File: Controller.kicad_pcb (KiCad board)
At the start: 4 copper layers, 180 x 80 mm, 39 parts, among them J1 I2C1, J10 I2C2, J11 MOTOR0_PWR, J12 MOTOR1_PWR, J13 MOTOR2_PWR, J14 MOTOR3_PWR, J15 MOTOR4_PWR, J16 MOTOR5_PWR, J17 ARM0_ROT, J18 ARM0_GRB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

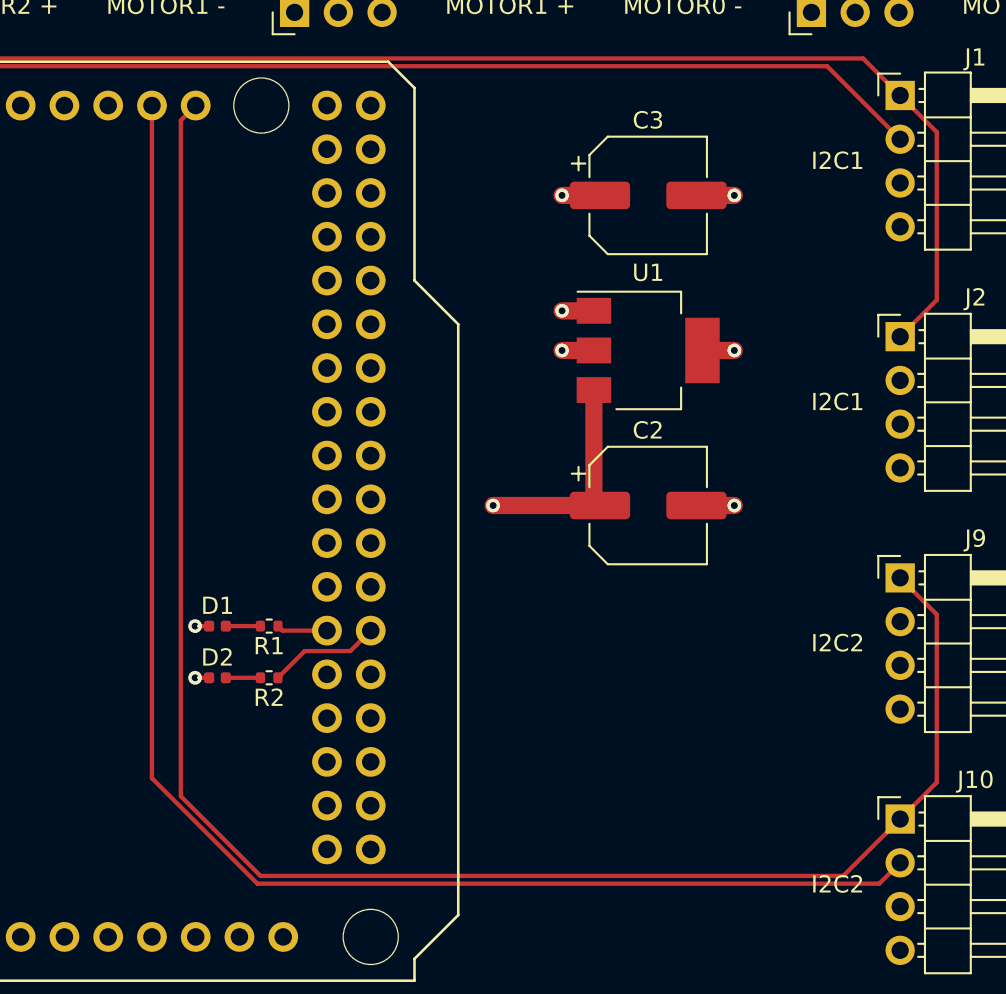
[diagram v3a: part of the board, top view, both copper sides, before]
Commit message: Use 0603 resistors and LED
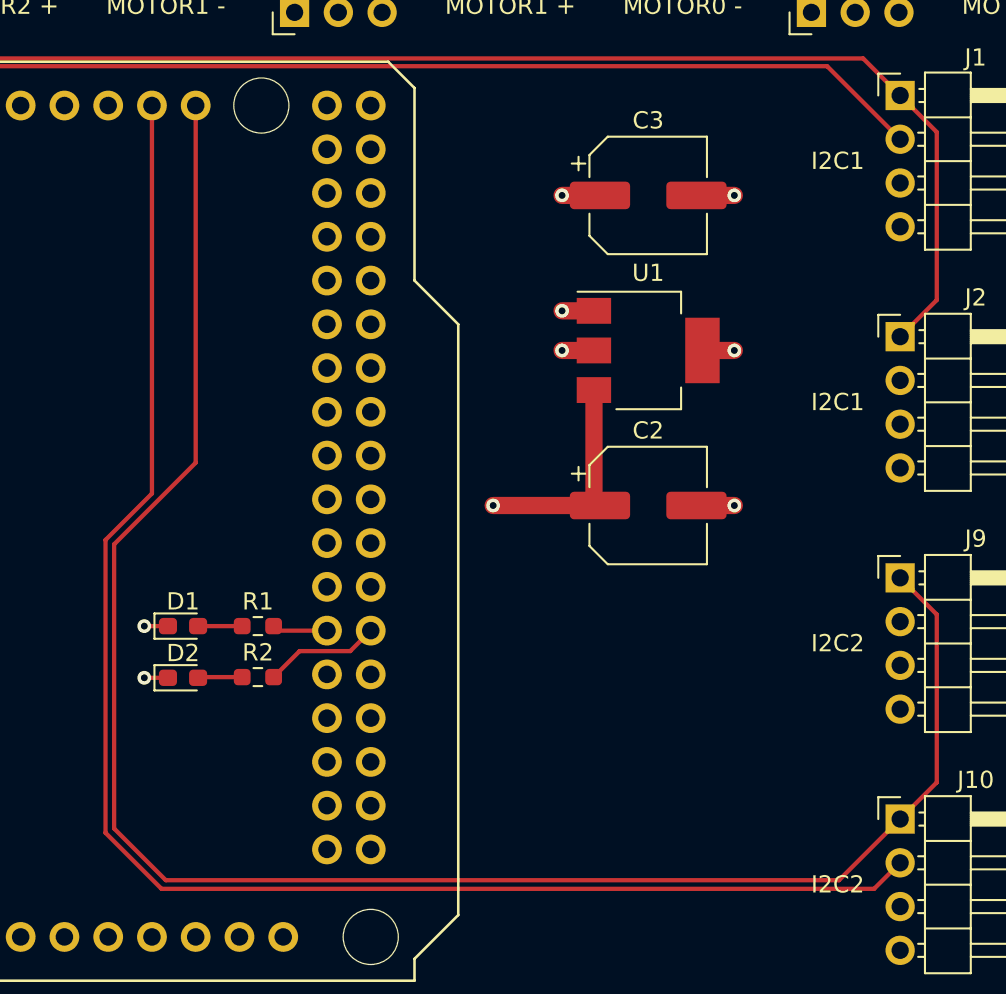
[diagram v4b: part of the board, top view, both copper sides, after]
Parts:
- D1, D2: footprint Diode_SMD:D_0402_1005Metric -> Diode_SMD:D_0603_1608Metric_Pad1.05x0.95mm_HandSolder
- R1, R2: footprint Resistor_SMD:R_0402_1005Metric -> Resistor_SMD:R_0603_1608Metric_Pad0.98x0.95mm_HandSolder
- moved D1 2.00 mm to (167.0, 86.0)
- moved D2 2.00 mm to (167.0, 89.0)
- moved R2 0.66 mm to (171.3, 89.0), turned to 0 degrees
- moved R1 0.66 mm to (171.3, 86.0), turned to 0 degrees
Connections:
- D1 pad 2: Net-(D1-Pad2) -> Net-(R1-Pad1)
- R1 pad 1: STATUS_RED -> Net-(R1-Pad1)
- R1 pad 2: Net-(D1-Pad2) -> STATUS_RED
- R2 pad 1: STATUS_GRN -> Net-(D2-Pad2)
- R2 pad 2: Net-(D2-Pad2) -> STATUS_GRN
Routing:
- net I2C2_SCL: track 101.2 -> 108.0 mm
- net I2C2_SDA: track 101.3 -> 107.2 mm
- net Net-(R1-Pad1): track 0.00 -> 2.56 mm
- net Net-(D1-Pad2): track 2.00 -> 0.00 mm
- net GND: track 14.8 -> 15.9 mm
- net Net-(D2-Pad2): track 2.00 -> 2.57 mm
